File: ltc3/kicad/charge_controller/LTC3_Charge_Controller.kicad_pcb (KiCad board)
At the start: 4 copper layers, 102 x 83 mm, 428 parts, among them P1 MicroFit header, P3 XH header, P4 MicroFit header, P5 XH header, P6 XH header, Q1 ZVN4525E6, Q2 BSC028N06NS, Q3 BSC028N06NS, Q4 BSC028N06NS, Q5 BSC028N06NS, Q6 ZVP3310F, Q7 MMBT5550L, U1 PI2127, U2 PI2127, U3 LT8490, U4 LTC2990

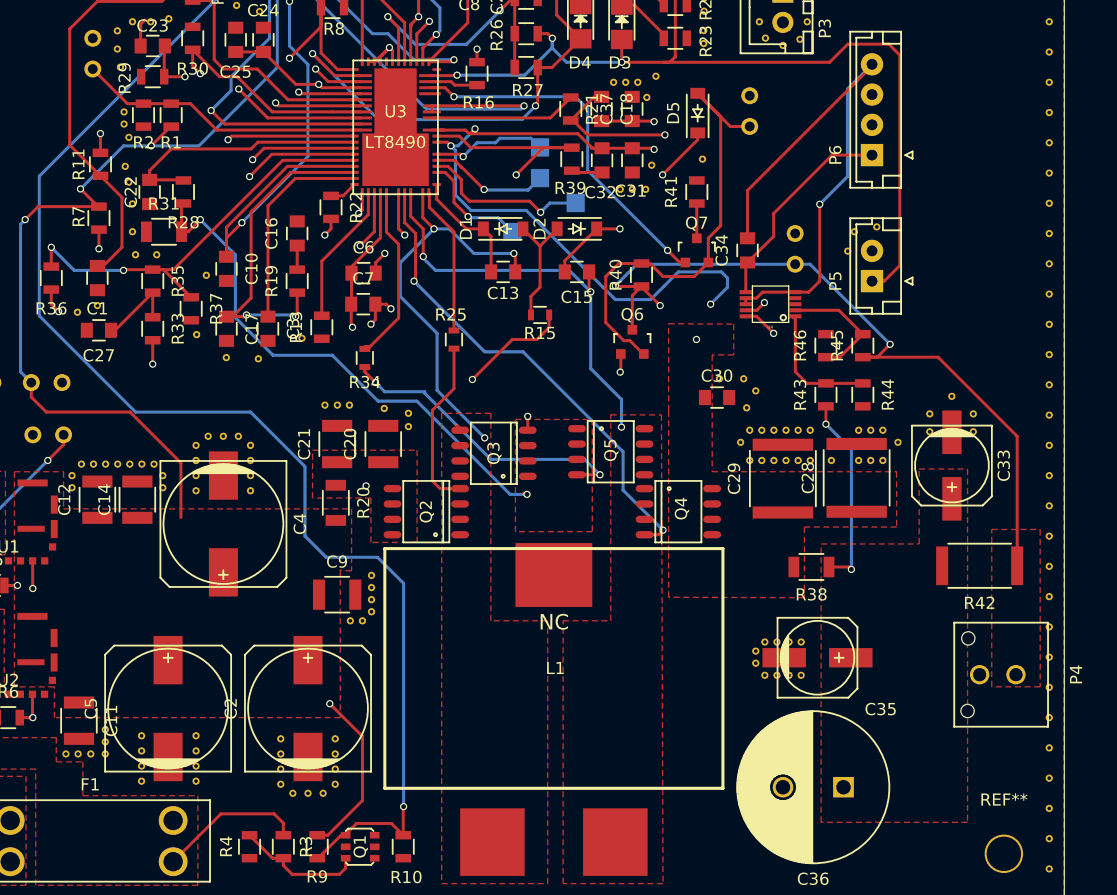
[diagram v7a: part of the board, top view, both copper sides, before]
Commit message: LTC3: Layout Review Notes & Small Changes
Added some changes from the layout review today.
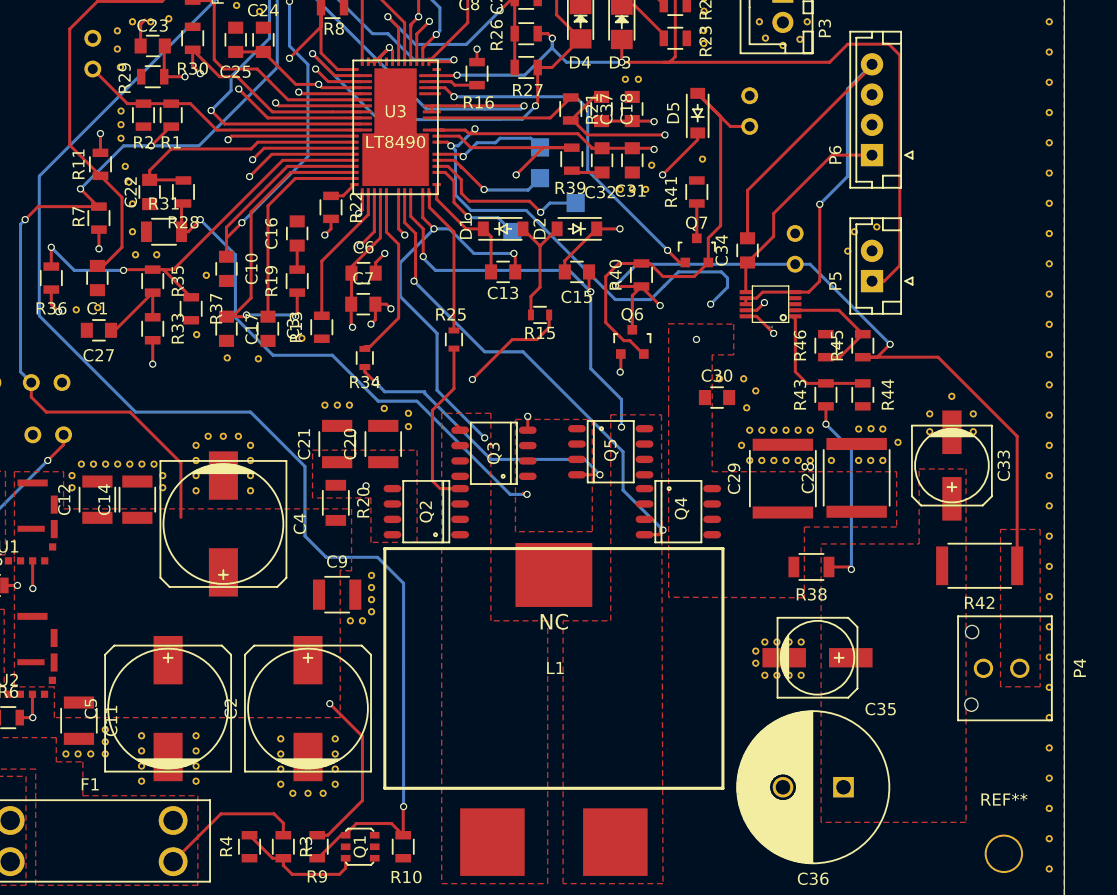
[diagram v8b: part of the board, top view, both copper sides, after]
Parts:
- removed the REF** at (157.2, 76.0)
- removed the REF** at (160.7, 75.5)
- removed the REF** at (160.0, 77.3)
- moved REF** 1.08 mm to (159.3, 75.8)
- moved REF** 1.06 mm to (158.2, 75.8)
- moved REF** 0.65 mm to (116.5, 80.7)
- moved P4 0.61 mm to (190.8, 124.5)
- moved REF** 0.26 mm to (167.8, 106.0)
- moved REF** 0.26 mm to (116.5, 78.4)
- moved REF** 0.25 mm to (116.5, 79.5)
- moved REF** 0.22 mm to (112.8, 94.8)
- moved REF** 0.18 mm to (114.6, 94.7)
- moved REF** 0.13 mm to (178.5, 104.7)
- moved REF** 0.10 mm to (179.5, 104.7)
- moved REF** 0.10 mm to (177.5, 104.7)
- moved REF** 0.08 mm to (125.3, 98.8)
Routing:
- net VIN: track 139.6 -> 140.1 mm
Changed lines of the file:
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@@
 (kicad_pcb (version 4) (host pcbnew "(2016-05-27 BZR 6836, Git 4441a4b)-product")
   (general
-    (links 581)
+    (links 579)
     (no_connects 0)
     (area 42.423199 60.5199 199.831029 145.9171)
     (thickness 1.6)
     (drawings 4)
-    (tracks 824)
+    (tracks 826)
     (zones 0)
-    (modules 428)
+    (modules 425)
     (nets 68)
   )
@@
   (layers
     (0 F.Cu signal)
-    (1 Ground.Plane signal hide)
-    (2 In2.Cu signal hide)
-    (31 B.Cu signal hide)
+    (1 Ground.Plane signal)
+    (2 In2.Cu signal)
+    (31 B.Cu signal)
     (32 B.Adhes user hide)
     (33 F.Adhes user)
@@
     (pad_to_mask_clearance 0)
     (aux_axis_origin 121.456 66.776)
-    (grid_origin 121.456 66.776)
-    (visible_elements 7FFFFFFF)
+    (grid_origin 199.731 119.801)
+    (visible_elements 7FFFFF7F)
     (pcbplotparams
       (layerselection 0x00030_ffffffff)
@@
   )
   (module LTC3:Via_.6mm (layer F.Cu)
-    (at 114.556 94.476)
+    (at 114.581 94.651)
     (fp_text reference REF** (at 0 1.27) (layer F.SilkS) hide
       (effects (font (size 1 1) (thickness 0.15)))
@@
   )
   (module LTC3:Via_.6mm (layer F.Cu)
-    (at 112.906 95.026)
+    (at 112.806 94.826)
     (fp_text reference REF** (at 0 1.27) (layer F.SilkS) hide
       (effects (font (size 1 1) (thickness 0.15)))
@@
   )
   (module LTC3:Via_.6mm (layer F.Cu)
-    (at 125.206 98.776)
+    (at 125.281 98.801)
     (fp_text reference REF** (at 0 1.27) (layer F.SilkS) hide
       (effects (font (size 1 1) (thickness 0.15)))
@@
   )
   (module LTC3:Via_.6mm (layer F.Cu)
-    (at 157.206 76.026)
+    (at 159.256 75.776)
     (fp_text reference REF** (at 0 1.27) (layer F.SilkS) hide
       (effects (font (size 1 1) (thickness 0.15)))
@@
   )
   (module LTC3:Via_.6mm (layer F.Cu)
-    (at 158.206 76.026)
+    (at 158.181 75.776)
     (fp_text reference REF** (at 0 1.27) (layer F.SilkS) hide
       (effects (font (size 1 1) (thickness 0.15)))
@@
   )
   (module LTC3:Via_.6mm (layer F.Cu)
-    (at 159.206 76.026)
-    (fp_text reference REF** (at 0 1.27) (layer F.SilkS) hide
-      (effects (font (size 1 1) (thickness 0.15)))
-    )
-    (fp_text value Via_.6mm (at 0 -1.27) (layer F.Fab) hide
-      (effects (font (size 1 1) (thickness 0.15)))
-    )
-    (pad 1 thru_hole circle (at 0 0) (size 0.6 0.6) (drill 0.3) (layers *.Cu)
-      (net 2 GND) (zone_connect 2))
-  )
-  (module LTC3:Via_.6mm (layer F.Cu)
-    (at 160.706 75.526)
-    (fp_text reference REF** (at 0 1.27) (layer F.SilkS) hide
-      (effects (font (size 1 1) (thickness 0.15)))
-    )
-    (fp_text value Via_.6mm (at 0 -1.27) (layer F.Fab) hide
-      (effects (font (size 1 1) (thickness 0.15)))
-    )
-    (pad 1 thru_hole circle (at 0 0) (size 0.6 0.6) (drill 0.3) (layers *.Cu)
-      (net 2 GND) (zone_connect 2))
-  )
-  (module LTC3:Via_.6mm (layer F.Cu)
-    (at 159.956 77.276)
-    (fp_text reference REF** (at 0 0) (layer F.SilkS) hide
-      (effects (font (size 1 1) (thickness 0.15)))
-    )
-    (fp_text value Via_.6mm (at 0 -1.27) (layer F.Fab) hide
-      (effects (font (size 1 1) (thickness 0.15)))
-    )
-    (pad 1 thru_hole circle (at 0 0) (size 0.6 0.6) (drill 0.3) (layers *.Cu)
-      (net 2 GND) (zone_connect 2))
-  )
-  (module LTC3:Via_.6mm (layer F.Cu)
     (at 160.356 82.876)
     (fp_text reference REF** (at 0 1.27) (layer F.SilkS) hide
@@
   )
   (module LTC3:Via_.6mm (layer F.Cu)
-    (at 167.706 105.776)
+    (at 167.781 106.026)
     (fp_text reference REF** (at 0 1.27) (layer F.SilkS) hide
       (effects (font (size 1 1) (thickness 0.15)))
@@
   )
   (module LTC3:Via_.6mm (layer F.Cu)
-    (at 179.456 104.776)
+    (at 179.456 104.676)
     (fp_text reference REF** (at 0 1.27) (layer F.SilkS) hide
       (effects (font (size 1 1) (thickness 0.15)))
@@
   )
   (module LTC3:Via_.6mm (layer F.Cu)
-    (at 178.456 104.776)
+    (at 178.481 104.651)
     (fp_text reference REF** (at 0 1.27) (layer F.SilkS) hide
       (effects (font (size 1 1) (thickness 0.15)))
@@
   )
   (module LTC3:Via_.6mm (layer F.Cu)
-    (at 177.456 104.776)
+    (at 177.456 104.676)
     (fp_text reference REF** (at 0 1.27) (layer F.SilkS) hide
       (effects (font (size 1 1) (thickness 0.15)))
@@
   )
   (module LTC3:Via_.6mm (layer F.Cu)
-    (at 117.156 80.576)
+    (at 116.506 80.651)
     (fp_text reference REF** (at 0 1.27) (layer F.SilkS) hide
       (effects (font (size 1 1) (thickness 0.15)))
@@
   )
   (module LTC3:Via_.6mm (layer F.Cu)
-    (at 116.756 78.476)
+    (at 116.506 78.401)
     (fp_text reference REF** (at 0 1.27) (layer F.SilkS) hide
       (effects (font (size 1 1) (thickness 0.15)))
@@
   )
   (module LTC3:Via_.6mm (layer F.Cu)
-    (at 116.756 79.476)
+    (at 116.506 79.526)
     (fp_text reference REF** (at 0 1.27) (layer F.SilkS) hide
       (effects (font (size 1 1) (thickness 0.15)))
@@
   )
   (module Connectors_Molex:Molex_Microfit3_Header_02x01_Straight_43045-0228 (layer F.Cu)
-    (at 190.456 124.976 90)
+    (at 190.771 124.451 90)
     (descr "Microfit3 Header Straight 02x01 43045-0228")
     (tags "connector Microfit 02x01 header straight 3mm")
@@
   (segment (start 137.942 73.894) (end 138.684 73.152) (width 0.25) (layer F.Cu) (net 2))
   (segment (start 163.3068 69.3572) (end 163.3068 69.596) (width 0.25) (layer F.Cu) (net 2))
-  (segment (start 151.356 75.776) (end 151.356 75.126) (width 0.25) (layer In2.Cu) (net 3))
-  (segment (start 149.8092 77.3228) (end 151.356 75.776) (width 0.25) (layer In2.Cu) (net 3))
-  (segment (start 160.556 76.476) (end 160.556 79.276) (width 0.25) (layer In2.Cu) (net 3))
-  (via (at 160.556 79.276) (size 0.6) (drill 0.4) (layers F.Cu B.Cu) (net 3))
-  (segment (start 160.556 79.276) (end 160.512 79.232) (width 0.25) (layer F.Cu) (net 3))
-  (segment (start 158.75 79.232) (end 160.512 79.232) (width 0.25) (layer F.Cu) (net 3))
-  (segment (start 149.8092 77.3228) (end 149.8092 77.978) (width 0.25) (layer In2.Cu) (net 3))
-  (segment (start 159.356 75.276) (end 160.556 76.476) (width 0.25) (layer In2.Cu) (net 3))
-  (segment (start 157.706 75.276) (end 159.356 75.276) (width 0.25) (layer In2.Cu) (net 3))
-  (segment (start 156.956 74.526) (end 157.706 75.276) (width 0.25) (layer In2.Cu) (net 3))
-  (segment (start 151.956 74.526) (end 156.956 74.526) (width 0.25) (layer In2.Cu) (net 3))
+  (segment (start 156.956 74.526) (end 157.031 74.526) (width 0.25) (layer In2.Cu) (net 3))
   (segment (start 151.356 75.126) (end 151.956 74.526) (width 0.25) (layer In2.Cu) (net 3))
+  (segment (start 151.956 74.526) (end 156.956 74.526) (width 0.25) (layer In2.Cu) (net 3))
+  (segment (start 149.8092 77.978) (end 149.8092 77.3228) (width 0.25) (layer In2.Cu) (net 3))
+  (segment (start 160.512 79.232) (end 158.75 79.232) (width 0.25) (layer F.Cu) (net 3))
+  (segment (start 160.556 79.276) (end 160.512 79.232) (width 0.25) (layer F.Cu) (net 3))
+  (via (at 160.556 79.276) (size 0.6) (drill 0.4) (layers F.Cu B.Cu) (net 3))
+  (segment (start 160.556 76.476) (end 160.556 79.276) (width 0.25) (layer In2.Cu) (net 3))
+  (segment (start 149.8092 77.3228) (end 151.356 75.776) (width 0.25) (layer In2.Cu) (net 3))
+  (segment (start 151.356 75.776) (end 151.356 75.126) (width 0.25) (layer In2.Cu) (net 3))
+  (segment (start 160.556 75.551) (end 160.556 76.476) (width 0.25) (layer In2.Cu) (net 3))
+  (segment (start 159.981 74.976) (end 160.556 75.551) (width 0.25) (layer In2.Cu) (net 3))
+  (segment (start 157.481 74.976) (end 159.981 74.976) (width 0.25) (layer In2.Cu) (net 3))
+  (segment (start 157.031 74.526) (end 157.481 74.976) (width 0.25) (layer In2.Cu) (net 3))
   (segment (start 158.75 79.232) (end 156.21 79.232) (width 0.25) (layer F.Cu) (net 3))
   (segment (start 142.192 78.473) (end 142.192 77.973) (width 0.25) (layer F.Cu) (net 3))
@@
     (polygon
       (pts
-        (xy 174.356 137.176) (xy 174.356 114.176) (xy 182.456 114.176) (xy 182.456 107.976) (xy 186.456 107.976)
-        (xy 186.456 137.176)
+        (xy 174.356 137.176) (xy 174.356 114.176) (xy 182.456 114.176) (xy 182.456 107.976) (xy 186.331 107.976)
+        (xy 186.331 137.176)
       )
     )
@@
     (polygon
       (pts
-        (xy 192.456 125.976) (xy 188.456 125.976) (xy 188.456 112.976) (xy 192.456 112.976) (xy 192.456 125.976)
+        (xy 192.456 125.976) (xy 189.181 125.976) (xy 189.181 112.976) (xy 192.456 112.976) (xy 192.456 125.976)
       )
     )
